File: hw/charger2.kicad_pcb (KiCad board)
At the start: 2 copper layers, 100 x 200 mm, 164 parts, among them J1 Fan, J4 4.5V Power Supply, J5 External ADS1115, Q1 AO3400, Q10 AO3400, Q11 AO3400, Q12 AO3400, Q13 AO3400, Q14 AO3400, Q15 AO3400, Q16 AO3400, Q17 AO3400, Q2 AO3400, Q3 AO3400, Q4 AO3400, Q5 AO3400, Q6 AO3400, Q7 AO3400, Q8 AO3400, Q9 AO3400, SW1 Button, U1 74HC4050, U10 TP4056, U12 MCP23017_SS, U15 74HC4052, U17 TP4056, U18 TP4056, U19 TP4056, U2 MCP23017_SS, U20 TP4056, U23 ADS1115, U3 2.2" SPI display, U4 74HC4052, U5 74HC4052, U7 TP4056, U8 TP4056, U9 TP4056

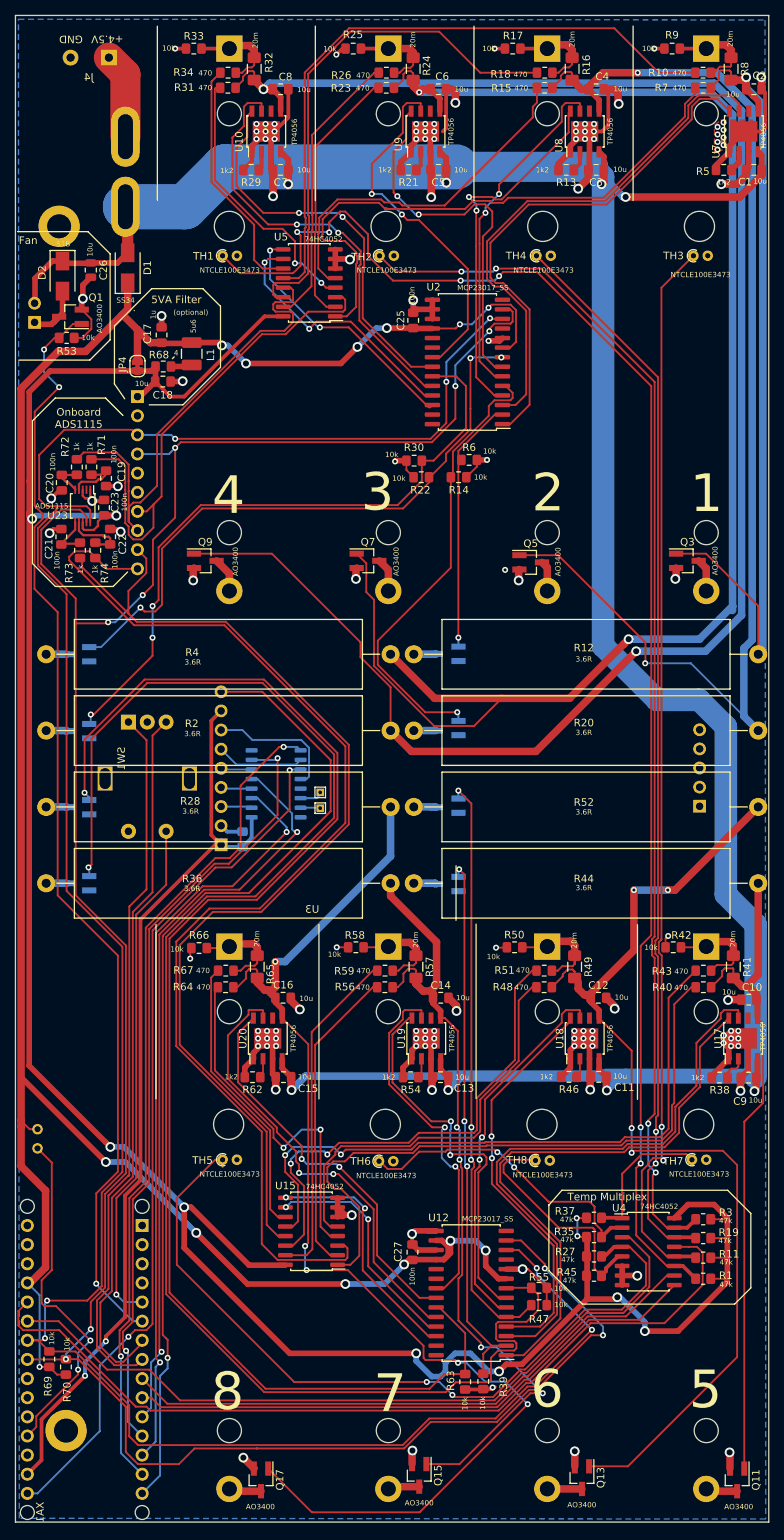
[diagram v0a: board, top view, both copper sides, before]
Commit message: fix 4052 footprint
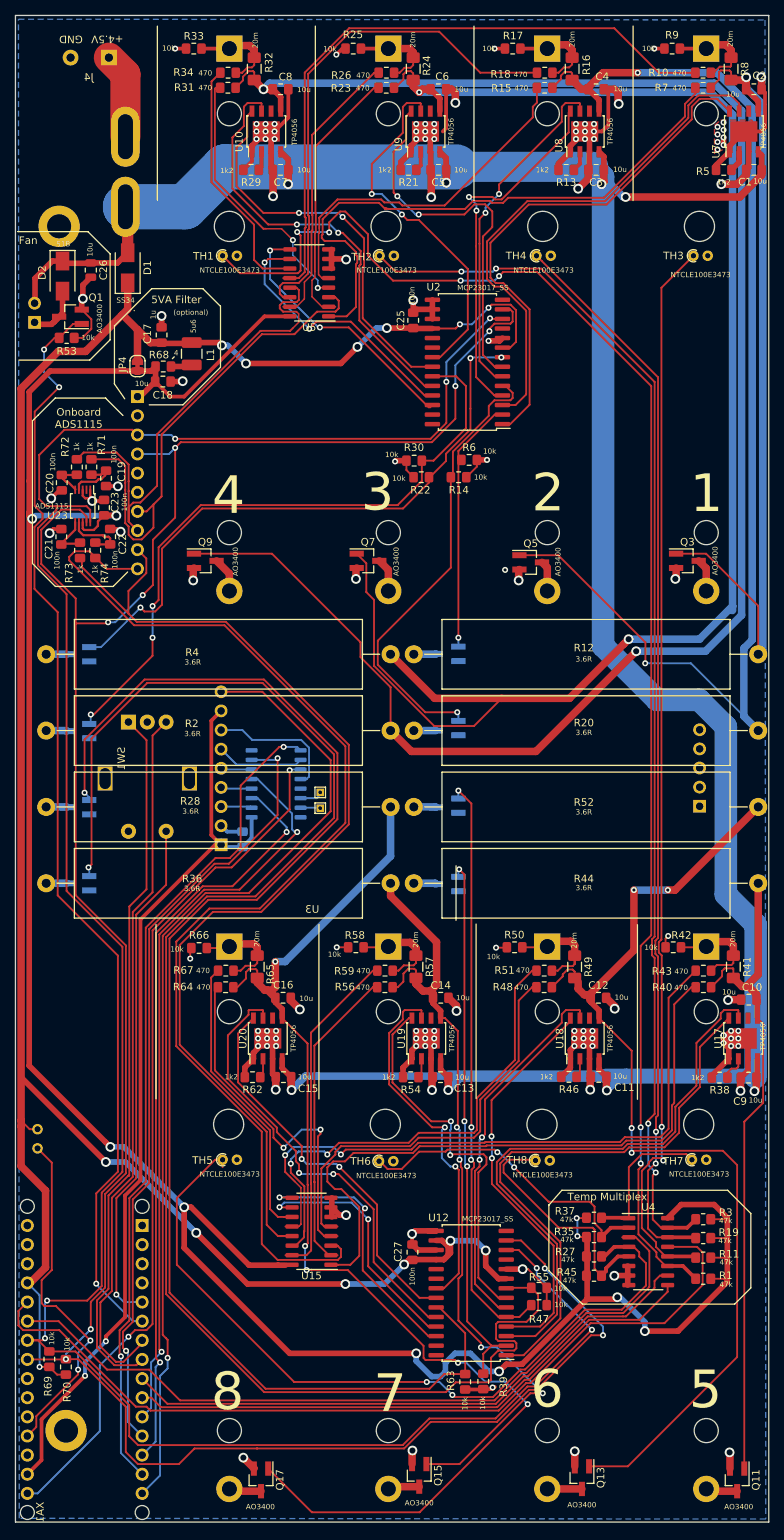
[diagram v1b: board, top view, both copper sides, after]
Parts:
- removed REF**: OSHW-Logo2_7.3x6mm_SilkScreen, Symbol:OSHW-Logo2_7.3x6mm_SilkScreen
- U15, U4, U5: footprint Package_SO:SO-16_5.3x10.2mm_P1.27mm -> Package_SO:SO-16_3.9x9.9mm_P1.27mm
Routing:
- net +5VA: track 341.2 -> 344.9 mm
- net Net-(U12-Pad26): track 32.9 -> 35.4 mm
- net Net-(U12-Pad25): track 30.8 -> 33.2 mm
- net /adc/AIN2: track 141.0 -> 142.8 mm
- net /quadcharger2/T1: track 19.3 -> 20.7 mm
- net /quadcharger2/X3: track 37.7 -> 38.8 mm
- net /adc/AIN0: track 67.7 -> 66.7 mm
- net /quadcharger1/X1: track 69.6 -> 68.6 mm
- net /adc/AIN3: track 156.8 -> 155.8 mm
- net /quadcharger1/Y2: track 34.8 -> 35.7 mm
- net /quadcharger2/Y0: track 85.8 -> 86.7 mm
- net /quadcharger2/T3: track 40.9 -> 41.8 mm
- net /quadcharger1/Y0: track 77.6 -> 78.5 mm
- net /quadcharger2/T2: track 31.3 -> 32.2 mm
- net /MCU/A7: track 114.4 -> 115.3 mm
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
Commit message: additional caps, groundplane improvements, MISO 3.3->5V
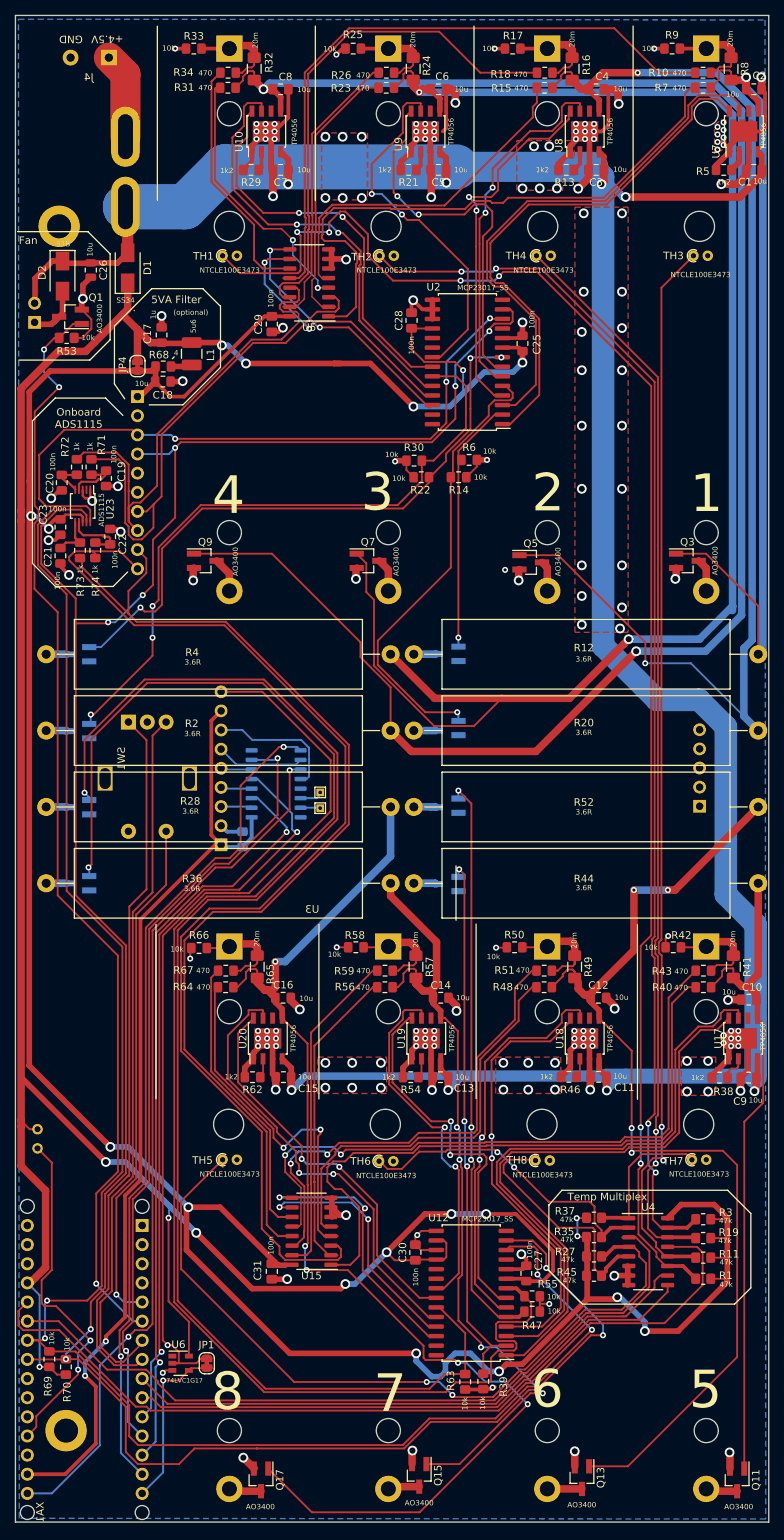
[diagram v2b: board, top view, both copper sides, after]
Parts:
- added C28: 100n, Capacitor_SMD:C_0805_2012Metric_Pad1.18x1.45mm_HandSolder, F.Cu at (40.2, 35.3)
- added C29: 100n, Capacitor_SMD:C_0805_2012Metric_Pad1.18x1.45mm_HandSolder, F.Cu at (21.6, 35.8)
- added C30: 100n, Capacitor_SMD:C_0805_2012Metric_Pad1.18x1.45mm_HandSolder, F.Cu at (40.7, 159.0)
- added C31: 100n, Capacitor_SMD:C_0805_2012Metric_Pad1.18x1.45mm_HandSolder, F.Cu at (21.6, 161.5)
- added JP1: MISO_JMP, Jumper:SolderJumper-2_P1.3mm_Bridged_RoundedPad1.0x1.5mm, F.Cu at (13.0, 173.7)
- added U6: 74LVC1G17, Package_TO_SOT_SMD:SOT-23-5, F.Cu at (9.53, 173.7)
- moved C27 15.4 mm to (55.4, 161.8)
- moved C25 14.8 mm to (54.9, 38.3)
- moved C23 6.34 mm to (-6.43, 62.7), turned to 270 degrees
- moved C21 2.52 mm to (-6.43, 66.5), turned to 270 degrees
- moved R55 1.45 mm to (56.2, 164.8)
- moved R47 1.25 mm to (56.2, 166.9)
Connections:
- net VCC renamed VDD
- U3 pad 9: /Display/MISO -> Net-(JP1-Pad2)
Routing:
- net Net-(JP1-Pad2): track 0.00 -> 117.8 mm, vias 0 -> 1
- net /Display/MISO: track 129.9 -> 22.6 mm
- net +5V: track 316.2 -> 379.2 mm
- net +5VA: track 344.9 -> 336.9 mm
- net +3V3: track 121.7 -> 125.9 mm
- net /quadcharger2/sheet5DC5D930/CE: track 53.9 -> 58.0 mm
- net GND: track 273.9 -> 277.7 mm, vias 121 -> 171
- net /quadcharger2/sheet5DC5D930/CHRG: track 49.7 -> 52.6 mm
- net /quadcharger2/sheet5DC5D9EA/DE: track 216.9 -> 214.0 mm
- net /quadcharger2/Battery/CHRG: track 78.7 -> 80.8 mm
- net /quadcharger2/Battery/CE: track 76.5 -> 78.5 mm
- net /quadcharger1/SCK: track 321.3 -> 323.2 mm
- net /quadcharger1/sheet5DC5D930/CHRG: track 45.8 -> 47.5 mm
- net /MCU/SDA: track 334.2 -> 335.5 mm
- net /quadcharger2/sheet5DC5D930/DE: track 78.4 -> 77.2 mm
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
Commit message: DRC fixes
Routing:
- net /quadcharger1/sheet5DC5D930/Bat+': track 162.5 -> 168.6 mm
- net /quadcharger1/Y0: track 78.2 -> 77.2 mm
- net /quadcharger1/sheet5DC5DB5C/CE: track 53.2 -> 52.6 mm
- net GND: vias 171 -> 169

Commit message: v0.2
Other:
- rule pad_to_mask_clearance: 0.051 -> 0
